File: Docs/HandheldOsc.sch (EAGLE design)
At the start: 16 parts, among them J1 BNC5-J-P-GN-RA-BH2D, U1 LMH6503MAX/NOPB, X1 SSW-106-02-G-D-RA, X2 SSW-105-02-G-D-RA

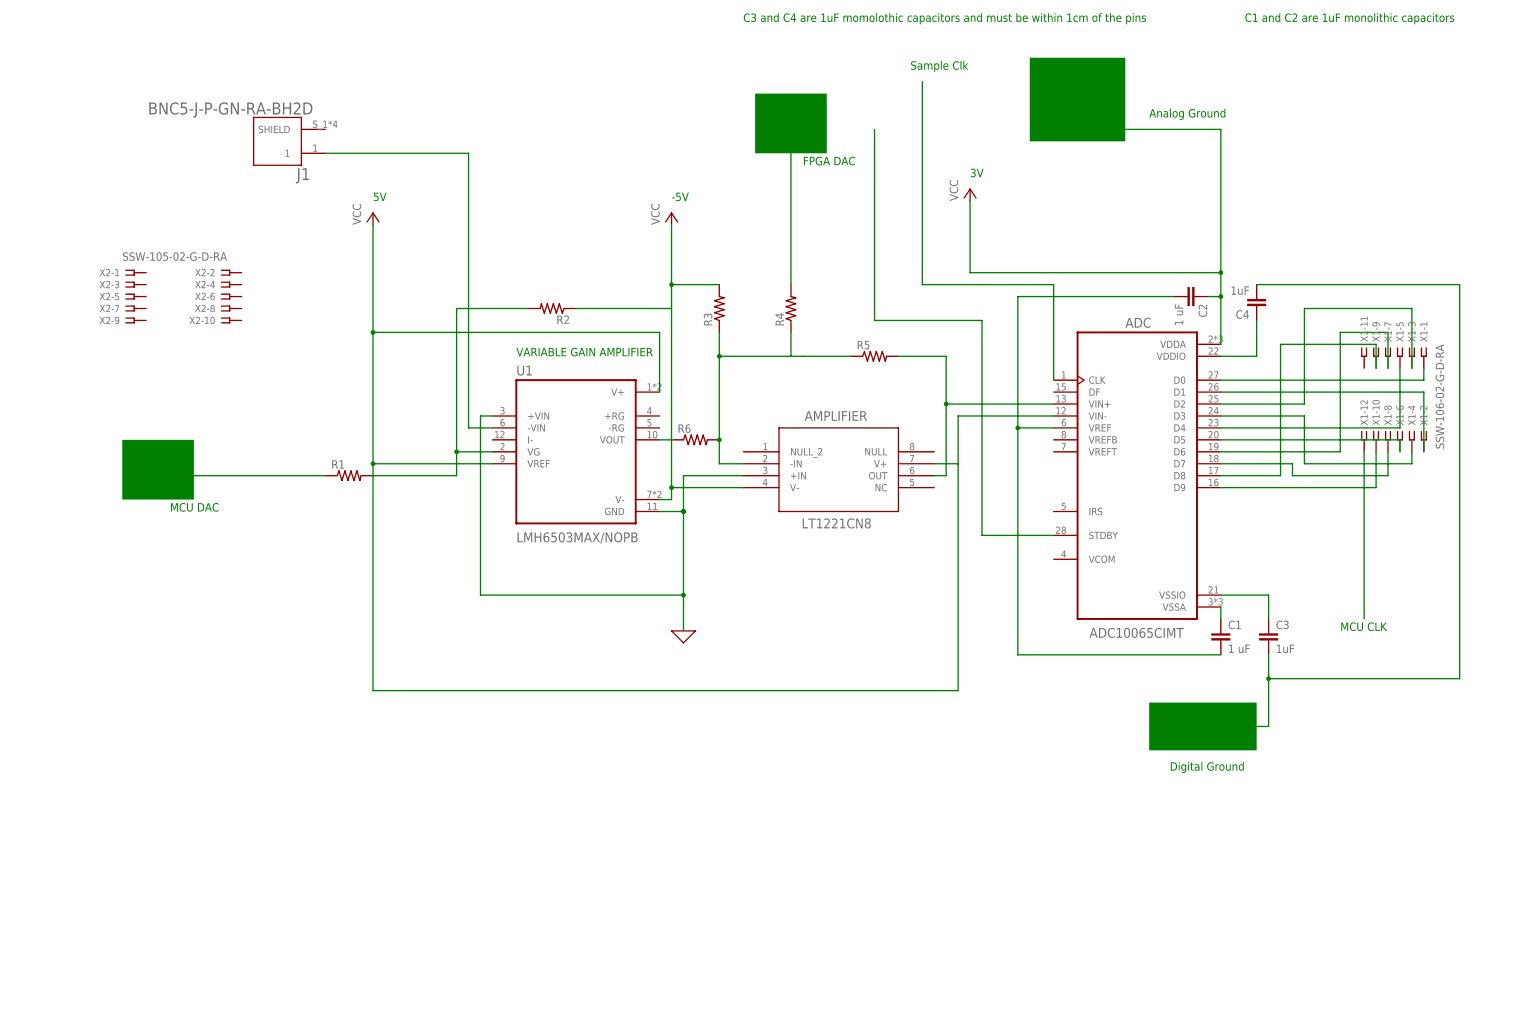
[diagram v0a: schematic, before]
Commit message: DAB Schematic V1.1
DAB Schematic V1.1 (order on JLCPCB)
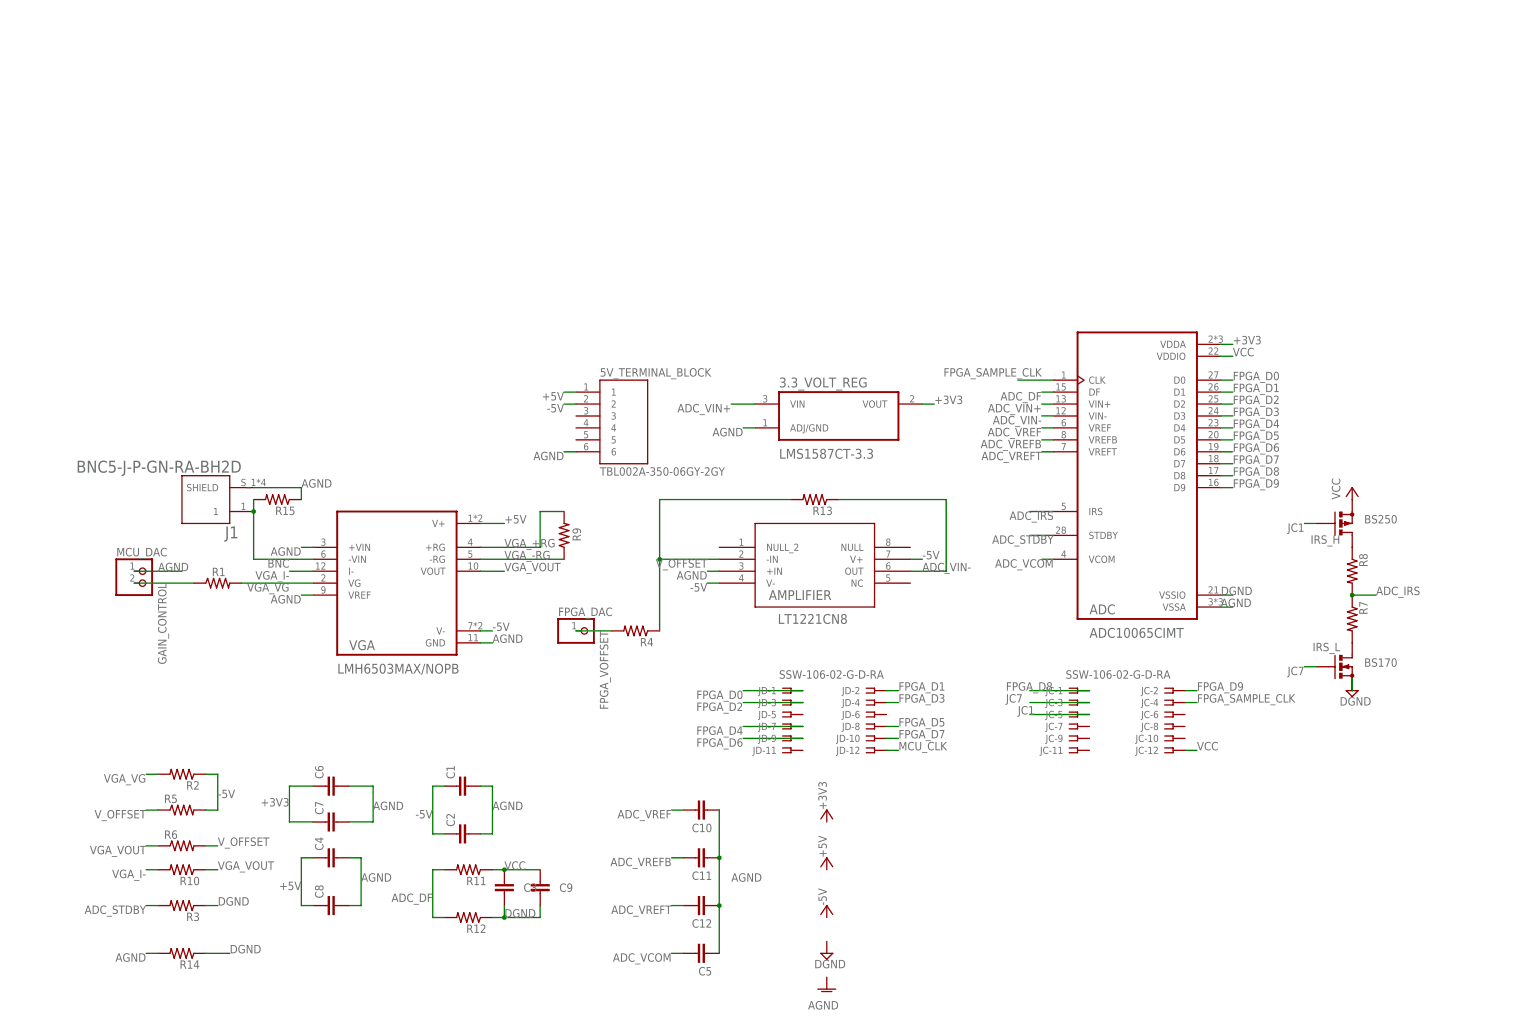
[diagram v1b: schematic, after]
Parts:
- removed U1: LMH6503MAX/NOPB, LMH6503MAX_NOPB:LMH6503MAX/NOPB
- removed X1: SSW-106-02-G-D-RA, con-samtec:SSW-106-02-G-D-RA
- removed X2: SSW-105-02-G-D-RA, con-samtec:SSW-105-02-G-D-RA
- added 3.3_VOLT_REG: LMS1587CT-3.3, LMS1587CT-3.3:LMS1587CT-3.3
- added 5V_TERMINAL_BLOCK: TBL002A-350-06GY-2GY, TBL002A-350-06GY-2GY:TBL002A-350-06GY-2GY
- added C10, C11, C12, C5, C6, C7, C8, C9: (no value), capacitor-wima:C2,5-3
- added FPGA_DAC: (no value), pinhead:PINHD-1X1
- added IRS_H: BS250, transistor-small-signal:BS250
- added IRS_L: BS170, transistor-small-signal:BS170
- added JC, JD: SSW-106-02-G-D-RA, con-samtec:SSW-106-02-G-D-RA
- added MCU_DAC: (no value), pinhead:PINHD-1X2
- added R10, R11, R12, R13, R14, R15, R7, R8, R9: (no value), rcl:R-US_0207/12
- added VGA: LMH6503MAX/NOPB, LMH6503MAX_NOPB:LMH6503MAX/NOPB
- C1, C2: value 1 uF -> (none)
- C3, C4: value 1uF -> (none)
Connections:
- removed net 0: AMPLIFIER.+IN, U1.+VIN, U1.GND
- removed net N$10: ADC.D2, X1-3.1
- removed net N$11: ADC.D3, X1-4.1
- removed net N$12: ADC.D4, X1-5.1
- removed net N$13: ADC.D5, X1-6.1
- removed net N$14: ADC.D6, X1-7.1
- removed net N$15: ADC.D7, X1-8.1
- removed net N$16: ADC.D8, X1-9.1
- removed net N$17: ADC.D9, X1-10.1
- removed net N$18: ADC.VREF, C1.2, C2.2
- removed net N$19: X1-12.1
- removed net N$20: ADC.STDBY
- removed net N$21: ADC.VSSA, C1.1
- removed net N$22: ADC.CLK
- removed net N$23: ADC.VDDIO, C4.1
- removed net N$24: C3.2, C4.2
- removed net N$25: ADC.VSSIO, C3.1
- removed net N$3: ADC.VIN+, AMPLIFIER.OUT, R5.2
- removed net N$4: R4.2
- removed net N$5: R1.1
- removed net N$6: J1.1, U1.-VIN
- removed net N$7: ADC.D0, X1-1.1
- removed net N$8: R1.2, R2.2, U1.VG
- removed net N$9: ADC.D1, X1-2.1
- new net +3V3: 3.3_VOLT_REG.VOUT, ADC.VDDA, C6.1, C7.1
- new net +5V: 5V_TERMINAL_BLOCK.1, C4.1, C8.1, VGA.V+
- new net -5V: 5V_TERMINAL_BLOCK.2, AMPLIFIER.V+, AMPLIFIER.V-, C1.1, C2.1, R2.1, R5.2, VGA.V-
- new net ADC_DF: ADC.DF, R11.2, R12.2
- new net ADC_IRS: ADC.IRS, R7.1, R8.2
- new net ADC_STDBY: ADC.STDBY, R3.2
- new net ADC_VCOM: ADC.VCOM, C5.1
- new net ADC_VIN+: 3.3_VOLT_REG.VIN, ADC.VIN+
- new net ADC_VIN-: ADC.VIN-, AMPLIFIER.OUT, R13.1
- new net ADC_VREF: ADC.VREF, C10.1
- new net ADC_VREFB: ADC.VREFB, C11.1
- new net ADC_VREFT: ADC.VREFT, C12.1
- new net AGND: 3.3_VOLT_REG.ADJ/GND, 5V_TERMINAL_BLOCK.6, ADC.VSSA, AMPLIFIER.+IN, C1.2, C10.2, C11.2, C12.2, C2.2, C4.2, C5.2, C6.2, C7.2, C8.2, J1.SHIELD, MCU_DAC.1, R14.2, R15.1, VGA.+VIN, VGA.GND, VGA.VREF
- new net BNC: J1.1, R15.2, VGA.-VIN
- new net DGND: ADC.VSSIO, C3.2, C9.2, IRS_L.S, R12.1, R14.1, R3.1
- new net FPGA_D0: ADC.D0, JD-1.1
- new net FPGA_D1: ADC.D1, JD-2.1
- new net FPGA_D2: ADC.D2, JD-3.1
- new net FPGA_D3: ADC.D3, JD-4.1
- new net FPGA_D4: ADC.D4, JD-7.1
- new net FPGA_D5: ADC.D5, JD-8.1
- new net FPGA_D6: ADC.D6, JD-9.1
- new net FPGA_D7: ADC.D7, JD-10.1
- new net FPGA_D8: ADC.D8, JC-1.1
- new net FPGA_D9: ADC.D9, JC-2.1
- new net FPGA_SAMPLE_CLK: ADC.CLK, JC-4.1
- new net FPGA_VOFFSET: FPGA_DAC.1, R4.2
- new net GAIN_CONTROL: MCU_DAC.2, R1.1
- new net JC1: IRS_H.G, JC-5.1
- new net JC7: IRS_L.G, JC-3.1
- new net MCU_CLK: JD-12.1
- new net VGA_+RG: R9.2, VGA.+RG
- new net VGA_-RG: R9.1, VGA.-RG
- new net VGA_I-: R10.2, VGA.I-
- new net VGA_VG: R1.2, R2.2, VGA.VG
- new net VGA_VOUT: R10.1, R6.1, VGA.VOUT
- new net V_OFFSET: AMPLIFIER.-IN, R13.2, R4.1, R5.1, R6.2
- net N$1: now also IRS_H.D, R8.1; no longer R6.1, U1.VOUT
- net N$2: now also IRS_L.D, R7.2; no longer AMPLIFIER.-IN, R3.1, R4.1, R5.1, R6.2
- net VCC: now also ADC.VDDIO, C3.1, C9.1, IRS_H.S, JC-12.1, R11.1; no longer ADC.VDDA, ADC.VIN-, AMPLIFIER.V+, AMPLIFIER.V-, C2.1, R2.1, R3.2, U1.V+, U1.V-, U1.VREF
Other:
- note removed: "-5V"
- note removed: "3V"
- note removed: "5V"
- note removed: "Analog Ground"
- note removed: "C1 and C2 are 1uF monolithic capacitors"
- note removed: "C3 and C4 are 1uF momolothic capacitors and must be within 1cm of the pins"
- note removed: "Digital Ground"
- note removed: "FPGA DAC"
- note removed: "MCU CLK"
- note removed: "MCU DAC"
- note removed: "Sample Clk"
- note removed: "VARIABLE GAIN AMPLIFIER"
- moved on the sheet: AMPLIFIER, C1, C2, C3, C4, J1, R1, R2, R3, R4, R5, R6
